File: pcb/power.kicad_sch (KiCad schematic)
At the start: 7 parts, among them J1 Conn_01x02_Pin, U3 AMS1117-3.3

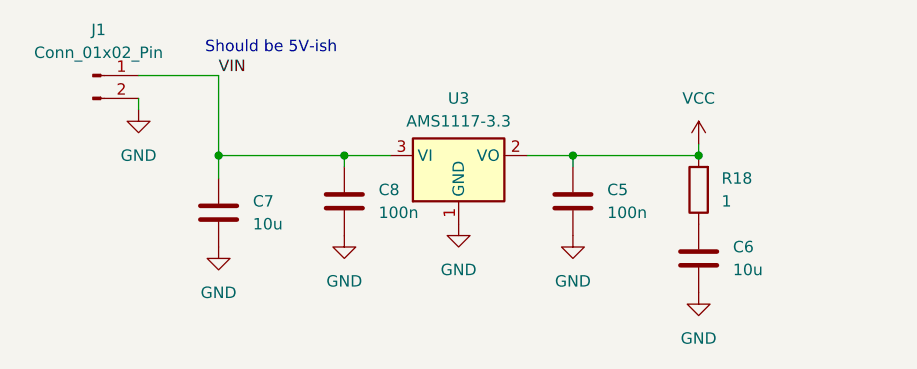
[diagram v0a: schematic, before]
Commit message: Route the basic elements + power + clk + rst network
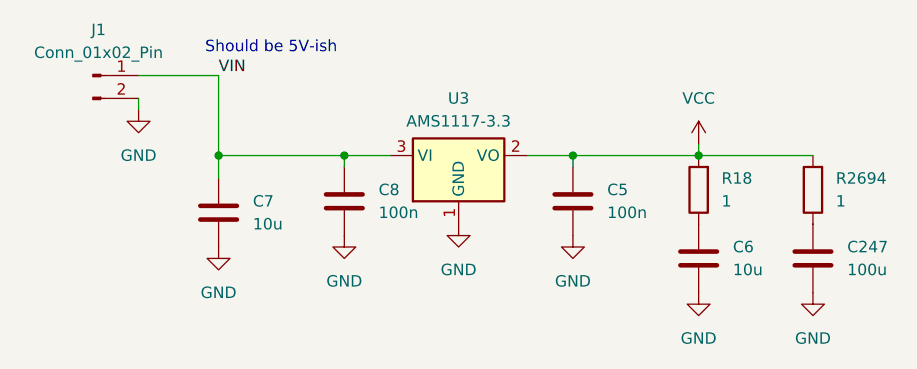
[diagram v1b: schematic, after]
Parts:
- added C247: 100u, Capacitor_SMD:C_1206_3216Metric, symbol Device:C
- added R2694: 1, Resistor_SMD:R_0402_1005Metric, symbol rflib:R
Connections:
- net GND: now also C247.2
- net VCC: now also R2694.2
- new net: C247.1, R2694.1
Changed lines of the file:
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@@
+	(wire
+		(pts
+			(xy 158.75 92.71) (xy 171.45 92.71)
+		)
+		(stroke
+			(width 0)
+			(type default)
+		)
+	)
 	(wire
 		(pts
@@
 	)
 	(symbol
+		(lib_id "rflib:R")
+		(at 171.45 96.52 180)
+		(unit 1)
+		(exclude_from_sim no)
+		(in_bom yes)
+		(on_board yes)
+		(dnp no)
+		(fields_autoplaced yes)
+		(property "Reference" "R2694"
+			(at 173.99 95.2499 0)
+			(effects
+				(font
+					(size 1.27 1.27)
+				)
+				(justify right)
+			)
+		)
+		(property "Value" "1"
+			(at 173.99 97.7899 0)
+			(effects
+				(font
+					(size 1.27 1.27)
+				)
+				(justify right)
+			)
+		)
+		(property "Footprint" "Resistor_SMD:R_0402_1005Metric"
+			(at 173.228 96.52 90)
+			(effects
+				(font
+					(size 1.27 1.27)
+				)
+				(hide yes)
+			)
+		)
+		(property "Datasheet" "~"
+			(at 171.45 96.52 0)
+			(effects
+				(font
+					(size 1.27 1.27)
+				)
+				(hide yes)
+			)
+		)
+		(property "Description" "Resistor"
+			(at 171.45 96.52 0)
+			(effects
+				(font
+					(size 1.27 1.27)
+				)
+				(hide yes)
+			)
+		)
+		(pin "2"
+		)
+		(pin "1"
+		)
+		(instances
+			(project "74aoc"
+				(path "/976aec4d-1ebe-44c6-a45c-c82e0c896ea2/4bf70d76-e048-47d6-b617-0a570812d98f"
+					(reference "R2694")
+					(unit 1)
+				)
+			)
+		)
+	)
+	(symbol
 		(lib_id "Device:C")
 		(at 158.75 104.14 0)
@@
 	)
 	(symbol
+		(lib_id "Device:C")
+		(at 171.45 104.14 0)
+		(unit 1)
+		(exclude_from_sim no)
+		(in_bom yes)
+		(on_board yes)
+		(dnp no)
+		(fields_autoplaced yes)
+		(property "Reference" "C247"
+			(at 175.26 102.8699 0)
+			(effects
+				(font
+					(size 1.27 1.27)
+				)
+				(justify left)
+			)
+		)
+		(property "Value" "100u"
+			(at 175.26 105.4099 0)
+			(effects
+				(font
+					(size 1.27 1.27)
+				)
+				(justify left)
+			)
+		)
+		(property "Footprint" "Capacitor_SMD:C_1206_3216Metric"
+			(at 172.4152 107.95 0)
+			(effects
+				(font
+					(size 1.27 1.27)
+				)
+				(hide yes)
+			)
+		)
+		(property "Datasheet" "~"
+			(at 171.45 104.14 0)
+			(effects
+				(font
+					(size 1.27 1.27)
+				)
+				(hide yes)
+			)
+		)
+		(property "Description" "Unpolarized capacitor"
+			(at 171.45 104.14 0)
+			(effects
+				(font
+					(size 1.27 1.27)
+				)
+				(hide yes)
+			)
+		)
+		(property "LCSC" "C15008"
+			(at 171.45 104.14 0)
+			(effects
+				(font
+					(size 1.27 1.27)
+				)
+				(hide yes)
+			)
+		)
+		(pin "1"
+		)
+		(pin "2"
+		)
+		(instances
+			(project "74aoc"
+				(path "/976aec4d-1ebe-44c6-a45c-c82e0c896ea2/4bf70d76-e048-47d6-b617-0a570812d98f"
+					(reference "C247")
+					(unit 1)
+				)
+			)
+		)
+	)
+	(symbol
 		(lib_id "Regulator_Linear:AMS1117-3.3")
 		(at 132.08 92.71 0)
@@
 					(unit 1)
 				)
+			)
+		)
+	)
+	(symbol
+		(lib_id "power:GND")
+		(at 171.45 107.95 0)
+		(unit 1)
+		(exclude_from_sim no)
+		(in_bom yes)
+		(on_board yes)
+		(dnp no)
+		(fields_autoplaced yes)
+		(property "Reference" "#PWR043"
+			(at 171.45 114.3 0)
+			(effects
+				(font
+					(size 1.27 1.27)
+				)
+				(hide yes)
+			)
+		)
+		(property "Value" "GND"
+			(at 171.45 113.03 0)
+			(effects
+				(font
+					(size 1.27 1.27)
+				)
+			)
+		)
+		(property "Footprint" ""
+			(at 171.45 107.95 0)
+			(effects
+				(font
+					(size 1.27 1.27)
+				)
+				(hide yes)
+			)
+		)
+		(property "Datasheet" ""
+			(at 171.45 107.95 0)
+			(effects
+				(font
+					(size 1.27 1.27)
+				)
+				(hide yes)
+			)
+		)
+		(property "Description" "Power symbol creates a global label with name \"GND\" , ground"
+			(at 171.45 107.95 0)
+			(effects
+				(font
+					(size 1.27 1.27)
+				)
+				(hide yes)
+			)
+		)
+		(pin "1"
+		)
+		(instances
+			(project "74aoc"
+				(path "/976aec4d-1ebe-44c6-a45c-c82e0c896ea2/4bf70d76-e048-47d6-b617-0a570812d98f"
+					(reference "#PWR043")
+					(unit 1)
+				)

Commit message: Add LCSC codes to everything that did not have them yet
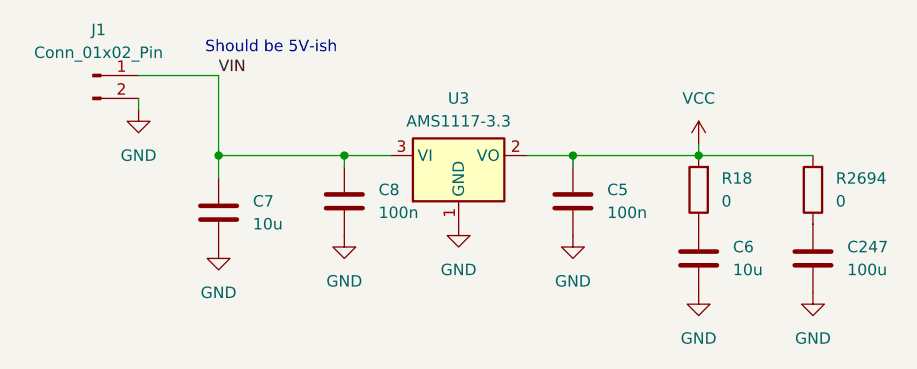
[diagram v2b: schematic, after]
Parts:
- C5, C8: LCSC (none) -> C1525
- C6, C7: LCSC (none) -> C19702
- R18, R2694: value 1 -> 0; LCSC (none) -> C17168
- U3: LCSC (none) -> C6186
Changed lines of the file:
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@@
 			)
 		)
-		(property "Value" "1"
+		(property "Value" "0"
 			(at 173.99 97.7899 0)
 			(effects
@@
 			)
 		)
+		(property "LCSC" "C17168"
+			(at 171.45 96.52 0)
+			(effects
+				(font
+					(size 1.27 1.27)
+				)
+				(hide yes)
+			)
+		)
 		(pin "2"
 		)
@@
 			)
 		)
+		(property "LCSC" "C19702"
+			(at 158.75 104.14 0)
+			(effects
+				(font
+					(size 1.27 1.27)
+				)
+				(hide yes)
+			)
+		)
 		(pin "1"
 		)
@@
 			)
 		)
+		(property "LCSC" "C6186"
+			(at 132.08 92.71 0)
+			(effects
+				(font
+					(size 1.27 1.27)
+				)
+				(hide yes)
+			)
+		)
 		(pin "3"
 		)
@@
 			)
 		)
+		(property "LCSC" "C19702"
+			(at 105.41 99.06 0)
+			(effects
+				(font
+					(size 1.27 1.27)
+				)
+				(hide yes)
+			)
+		)
 		(pin "1"
 		)
@@
 			)
 		)
+		(property "LCSC" "C1525"
+			(at 119.38 97.79 0)
+			(effects
+				(font
+					(size 1.27 1.27)
+				)
+				(hide yes)
+			)
+		)
 		(pin "1"
 		)
@@
 			)
 		)
+		(property "LCSC" "C1525"
+			(at 144.78 97.79 0)
+			(effects
+				(font
+					(size 1.27 1.27)
+				)
+				(hide yes)
+			)
+		)
 		(pin "1"
 		)
@@
 			)
 		)
-		(property "Value" "1"
+		(property "Value" "0"
 			(at 161.29 97.7899 0)
 			(effects
@@
 			(at 158.75 96.52 0)
 			(effects
+				(font
+					(size 1.27 1.27)
+				)
+				(hide yes)
+			)
+		)
+		(property "LCSC" "C17168"
+			(at 158.75 96.52 0)
+			(effects
